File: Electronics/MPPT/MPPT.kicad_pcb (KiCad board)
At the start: 2 copper layers, 152.4 x 119.4 mm, 128 parts, among them J1 Solar Array, J2 Battery, J3 Car Power, J4 CAN_In, J5 CAN_Out, Q1 200N25N, Q2 200N25N, SW1 RESET, SW2 CAN Address, U1 PQMC3-D12-S9-S, U2 Nucleo_L432KC, U3 UCC37321, U4 INA210, U5 ADM3055E, U6 INA210, U7 CDSOT23-T24CAN

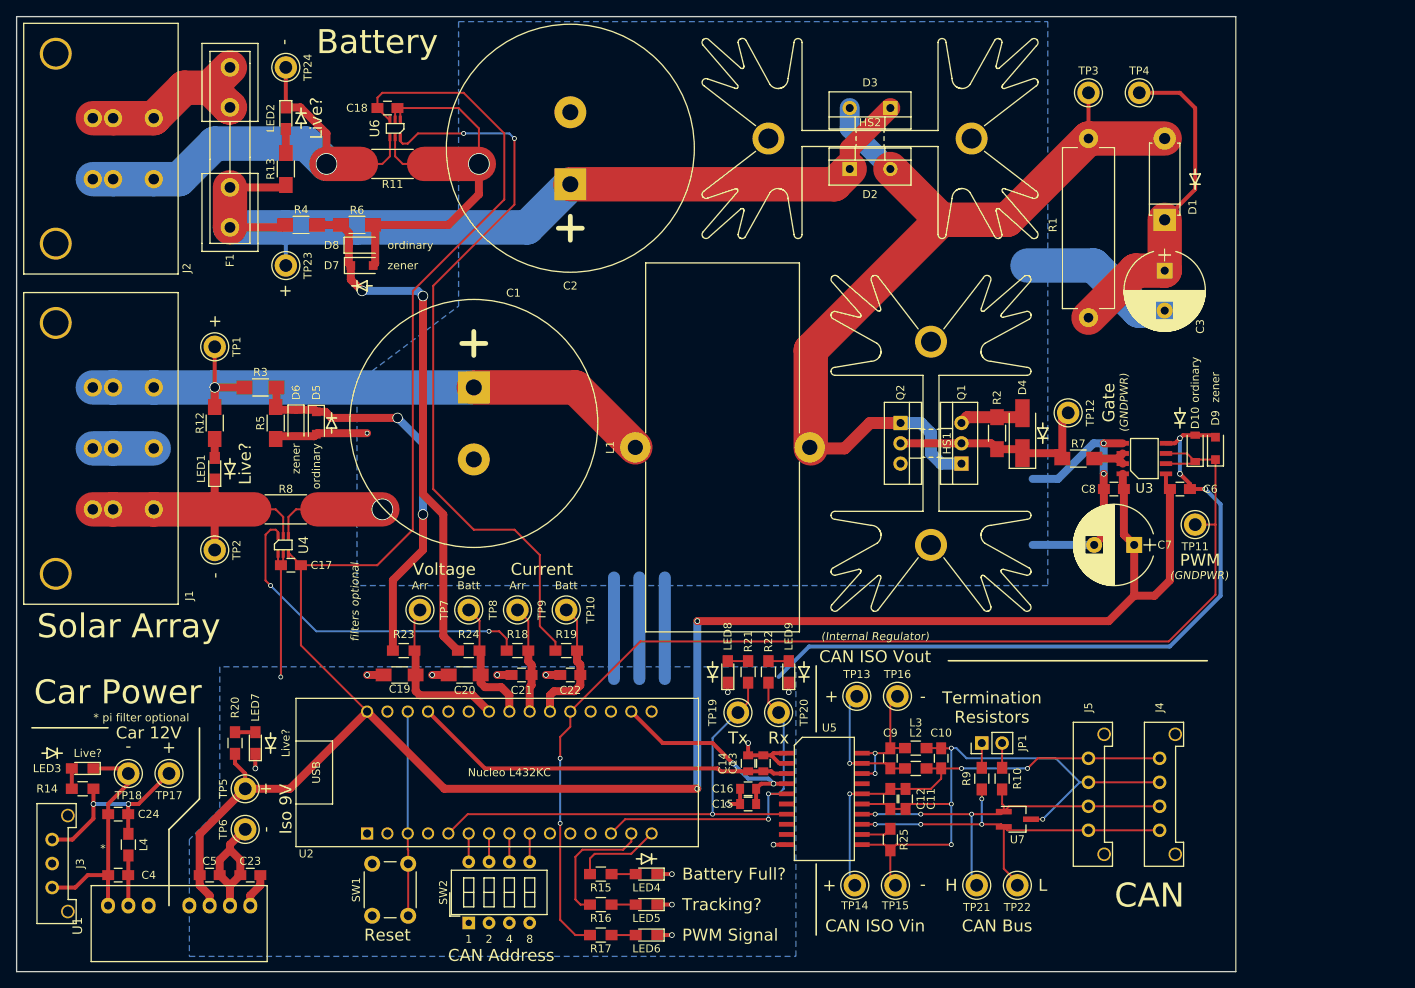
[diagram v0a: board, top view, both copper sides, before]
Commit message: MPPT: Fill GND planes
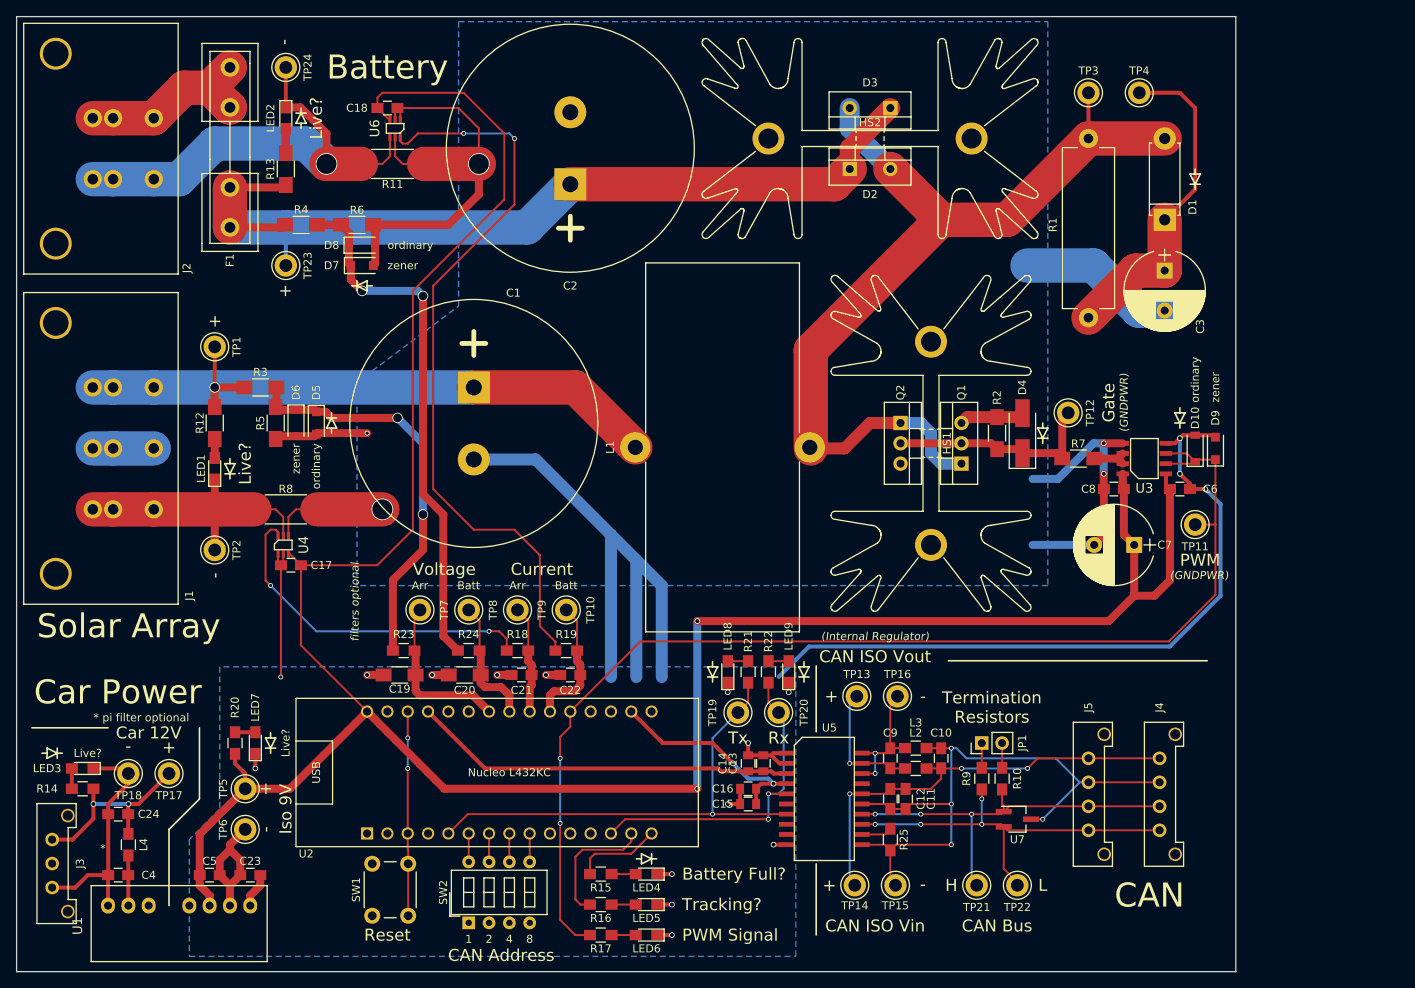
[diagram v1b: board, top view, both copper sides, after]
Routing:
- net GNDPWR: track 297.7 -> 372.2 mm
- net (no net): track 38.1 -> 0.00 mm
- net /Reset: vias 0 -> 2

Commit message: MPPT: Further compact board
Saved ~.6 sq in
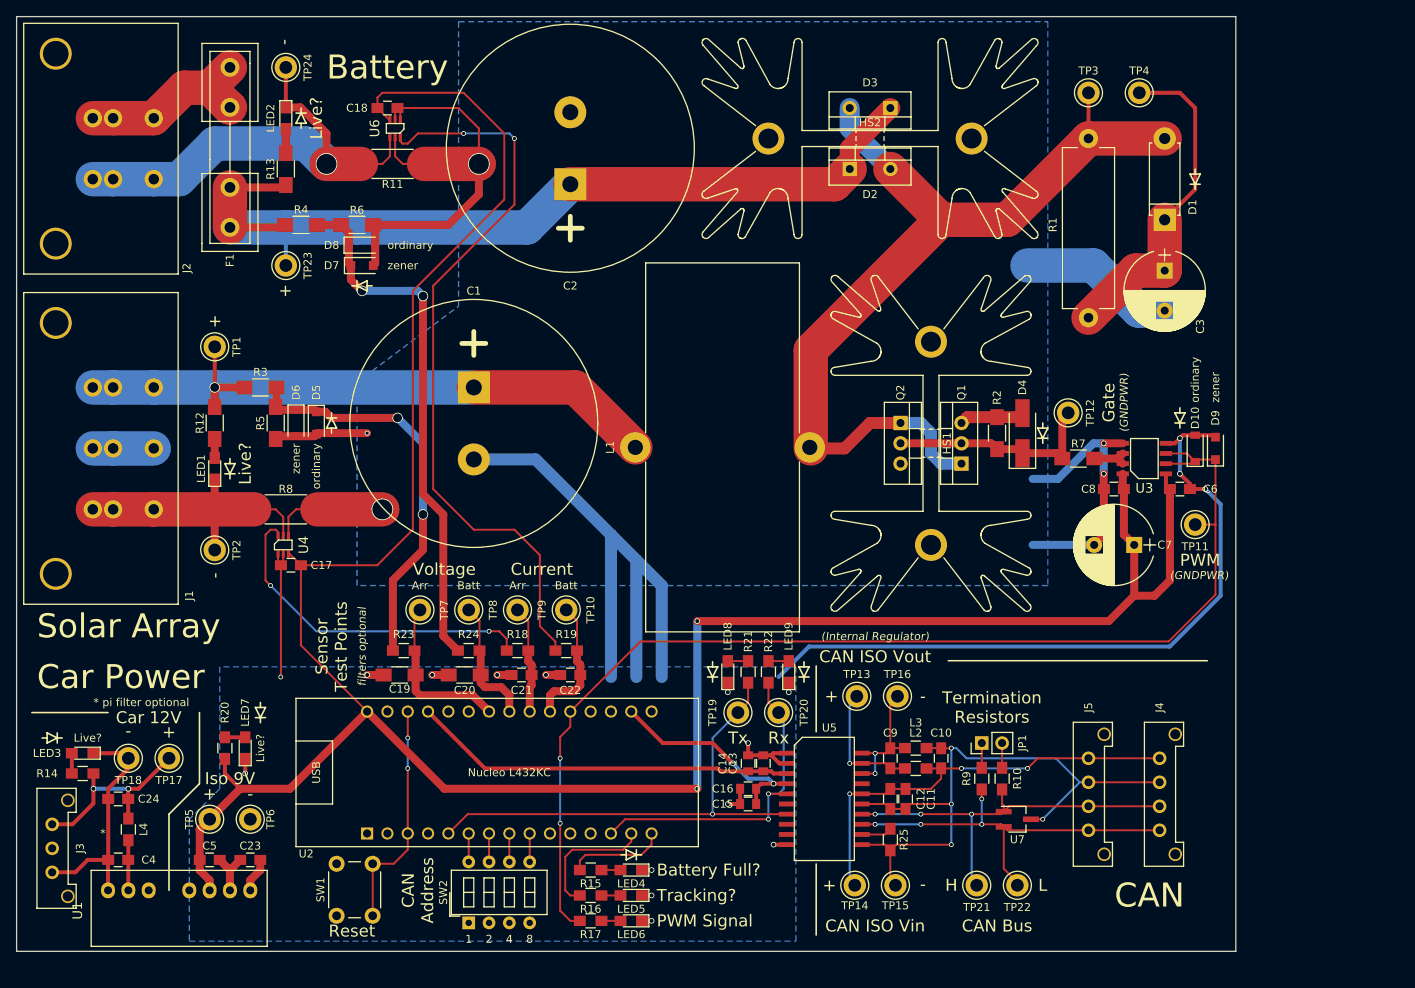
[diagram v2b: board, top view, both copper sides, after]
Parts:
- moved TP5 5.85 mm to (55.2, 131.4), turned to 180 degrees
- moved SW1 4.44 mm to (71.1, 143.5)
- moved REF** 4.02 mm to (61.6, 118.1)
- moved LED6 2.61 mm to (108.0, 144.1)
- moved LED5 2.22 mm to (108.0, 141.0)
- moved R17 2.18 mm to (102.9, 144.1)
- moved LED4 1.97 mm to (108.0, 137.8)
- moved REF** 1.97 mm to (108.0, 135.9)
- moved C23 1.91 mm to (60.3, 136.5)
- moved C24 1.91 mm to (43.8, 128.9)
- moved C4 1.91 mm to (43.8, 136.5)
- moved C5 1.91 mm to (55.2, 136.5)
- moved J3 1.91 mm to (35.6, 132.1)
- moved L4 1.91 mm to (45.1, 132.7)
- moved LED3 1.91 mm to (39.4, 123.2)
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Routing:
- net GNDPWR: track 372.2 -> 359.5 mm
- net /Reset: track 25.5 -> 28.9 mm
- net /PWM: track 147.7 -> 145.0 mm
- net +9VA: track 314.0 -> 312.1 mm
- net /Battery_Full: track 10.9 -> 12.4 mm
- net Net-(LED6-Pad2): track 3.02 -> 2.38 mm
- net Net-(LED5-Pad2): track 3.02 -> 2.38 mm
- net Net-(LED4-Pad2): track 3.02 -> 2.38 mm
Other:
- board size 152.4 x 119.4 mm -> 152.4 x 116.8 mm
- board text added: "Sensor Test Points"

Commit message: MPPT: Add ground TPs for sensors, snubber, and FET driver.
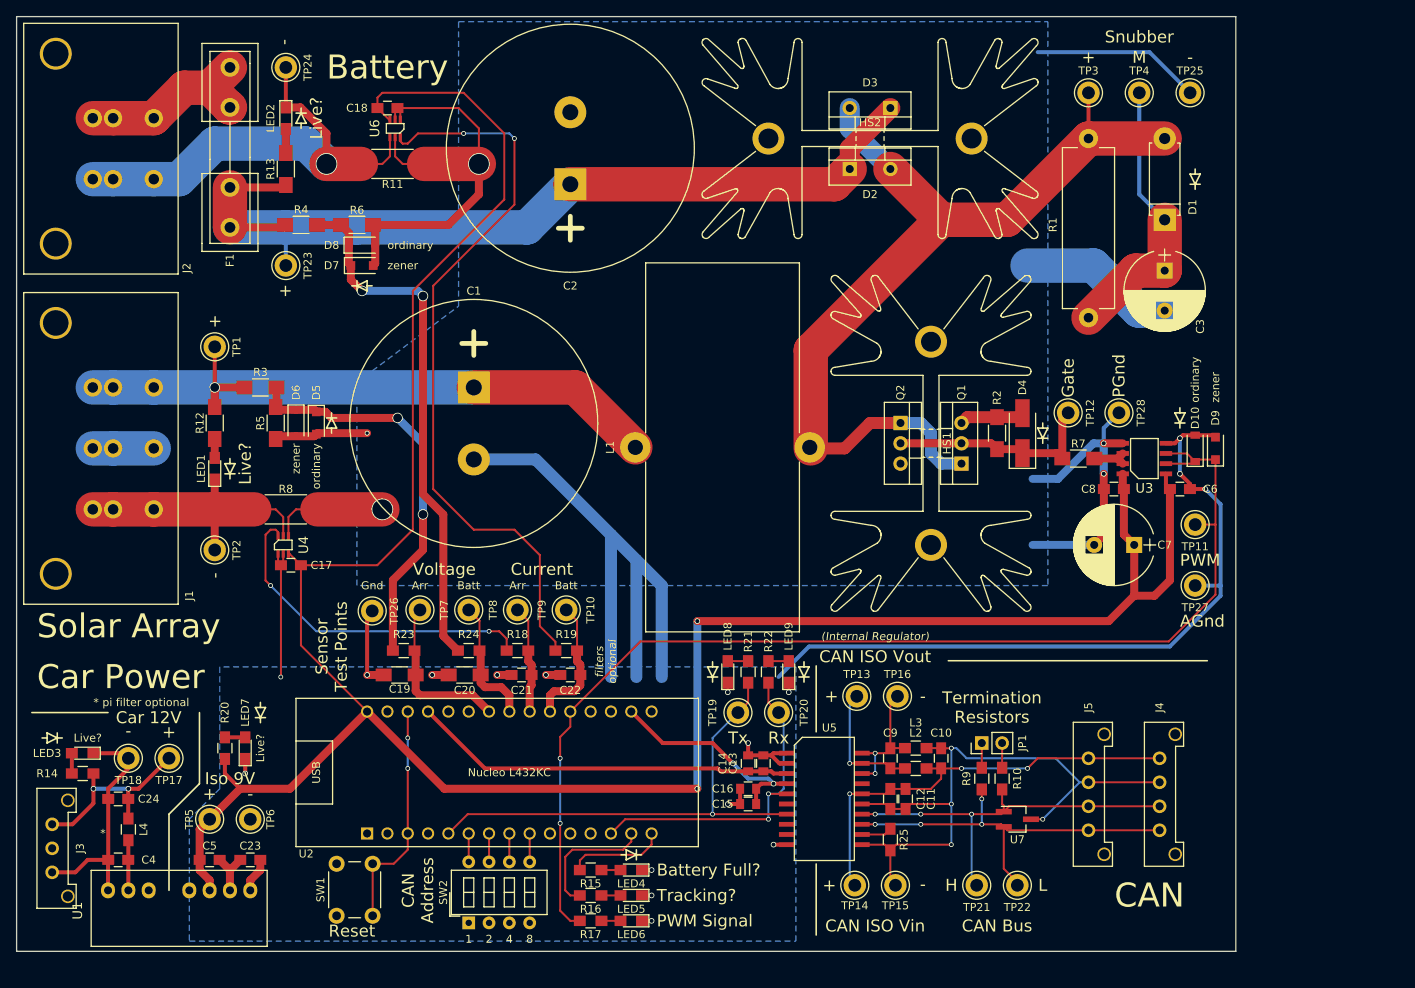
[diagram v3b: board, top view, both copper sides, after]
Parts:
- added TP25: -SNUB, Measurement_Points:Test_Point_Keystone_5005-5009_Compact, F.Cu at (177.8, 40.6)
- added TP26: GND, Measurement_Points:Test_Point_Keystone_5005-5009_Compact, F.Cu at (75.6, 105.4)
- added TP27: AGND, Measurement_Points:Test_Point_Keystone_5005-5009_Compact, F.Cu at (178.4, 102.2)
- added TP28: PGND, Measurement_Points:Test_Point_Keystone_5005-5009_Compact, F.Cu at (168.9, 80.6)
- TP4: value SNUB_MID -> M_SNUB
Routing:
- net GNDPWR: track 359.5 -> 396.7 mm
- net Net-(C3-Pad1): track 41.6 -> 35.5 mm
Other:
- board text added: "AGnd"
- board text added: "Gnd"
- board text added: "M"
- board text added: "PGnd"
- board text added: "Snubber"
- board text removed: "(GNDPWR)"

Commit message: MPPT: Use more appropriate footprints for snubber components; rearrange that portion of board.
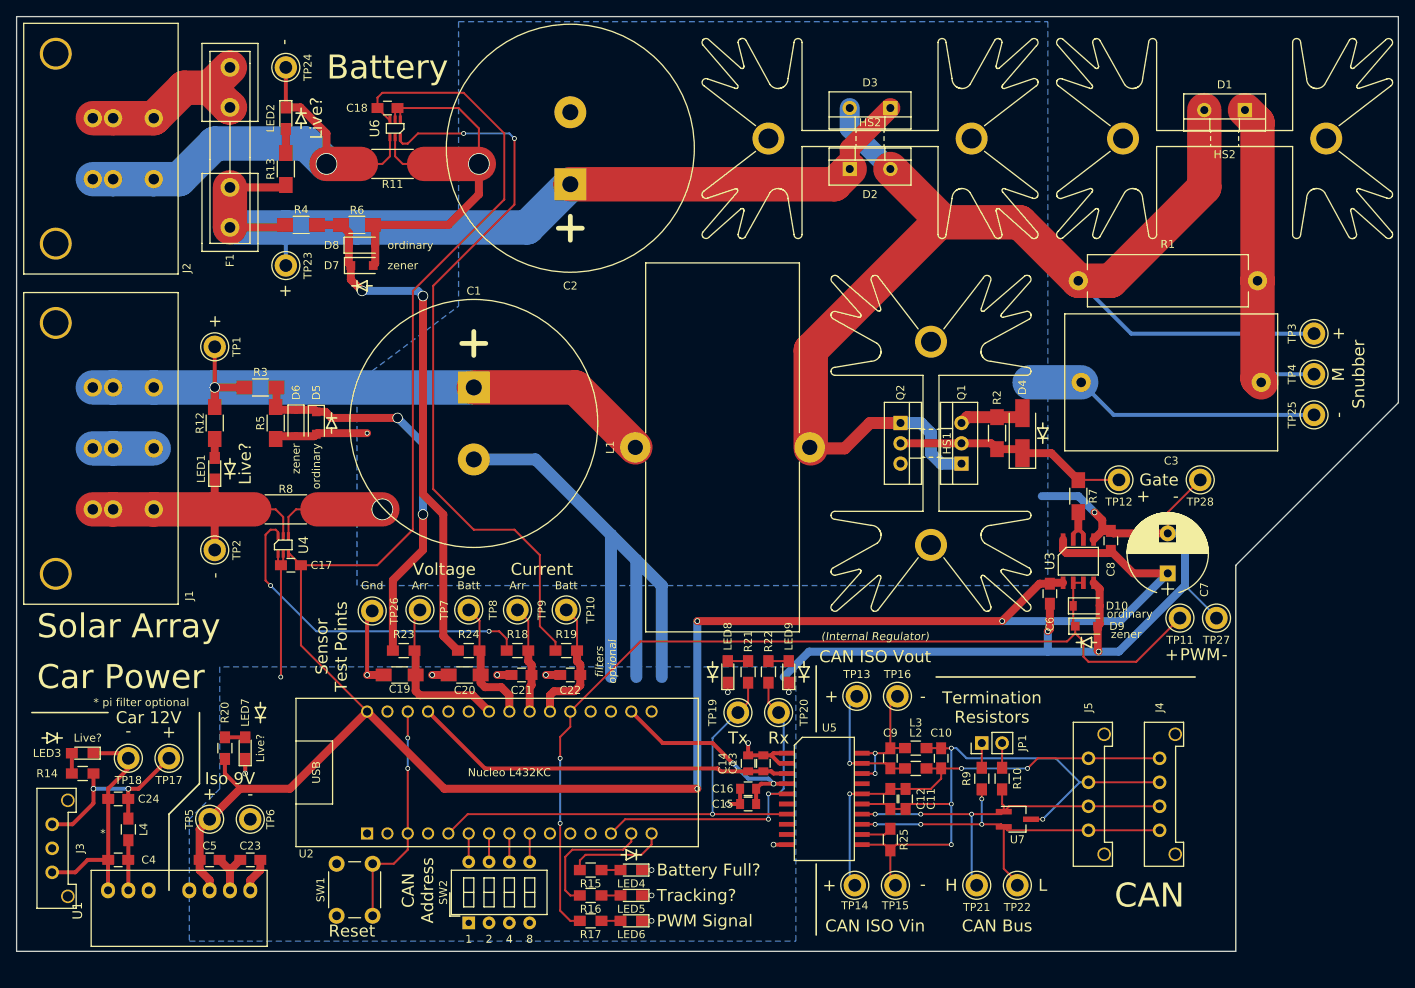
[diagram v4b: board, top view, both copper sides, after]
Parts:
- removed the REF** at (178.4, 51.4)
- added HS2: Heatsink_Fischer_SK129-STS_42x25mm_2xDrill2.5mm, Heatsinks:Heatsink_Fischer_SK129-STS_42x25mm_2xDrill2.5mm, F.Cu at (182.1, 46.4)
- C3: footprint Capacitors_THT:CP_Radial_D10.0mm_P5.00mm -> MPPT_Custom:C_Rect_L26.5mm_W17.0mm_P22.50mm_MKS4
- D1: value Diode -> Schottky; footprint Diodes_THT:D_5W_P10.16mm_Horizontal -> TO_SOT_Packages_THT:TO-220-2_Vertical
- moved TP25 43.1 mm to (193.3, 80.9), turned to 90 degrees
- moved TP4 41.4 mm to (193.3, 75.8), turned to 90 degrees
- moved TP3 41.2 mm to (193.3, 70.7), turned to 90 degrees
- moved REF** 30.4 mm to (164.8, 109.3), turned to 90 degrees
- moved D9 27.5 mm to (164.8, 107.3), turned to 0 degrees
- moved D10 23.9 mm to (164.8, 104.8), turned to 0 degrees
- moved C6 20.9 mm to (160.3, 103.3), turned to 90 degrees
- moved C3 18.5 mm to (186.7, 76.8), turned to 180 degrees
- moved R1 17.8 mm to (163.8, 64.1), turned to 0 degrees
- moved D1 17.0 mm to (184.7, 42.8), turned to 180 degrees
- moved U3 15.3 mm to (163.8, 99.2), turned to 0 degrees
- moved TP28 13.2 mm to (179.1, 89.0), turned to 180 degrees
- moved TP11 11.8 mm to (176.5, 106.3)
- moved TP12 10.5 mm to (168.9, 89.0), turned to 180 degrees
- moved C8 6.49 mm to (167.9, 96.6), turned to 90 degrees
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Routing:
- net Net-(D1-Pad2): track 115.6 -> 160.7 mm
- net /PWM: track 145.0 -> 121.2 mm
- net GNDPWR: track 396.7 -> 374.8 mm, vias 22 -> 20
- net Net-(C3-Pad1): track 35.5 -> 41.9 mm
- net +9VA: track 312.1 -> 308.3 mm, vias 2 -> 3
- net /Drive_PWM: track 27.1 -> 29.2 mm
- net Net-(R7-Pad2): track 4.72 -> 5.32 mm
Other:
- board size 152.4 x 116.8 mm -> 172.7 x 116.8 mm
- board text removed: "AGnd"
- board text removed: "PGnd"

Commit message: MPPT: Correct fuse footprint.
We had been using a placeholder for a while, but I've now verified the correct footprint.
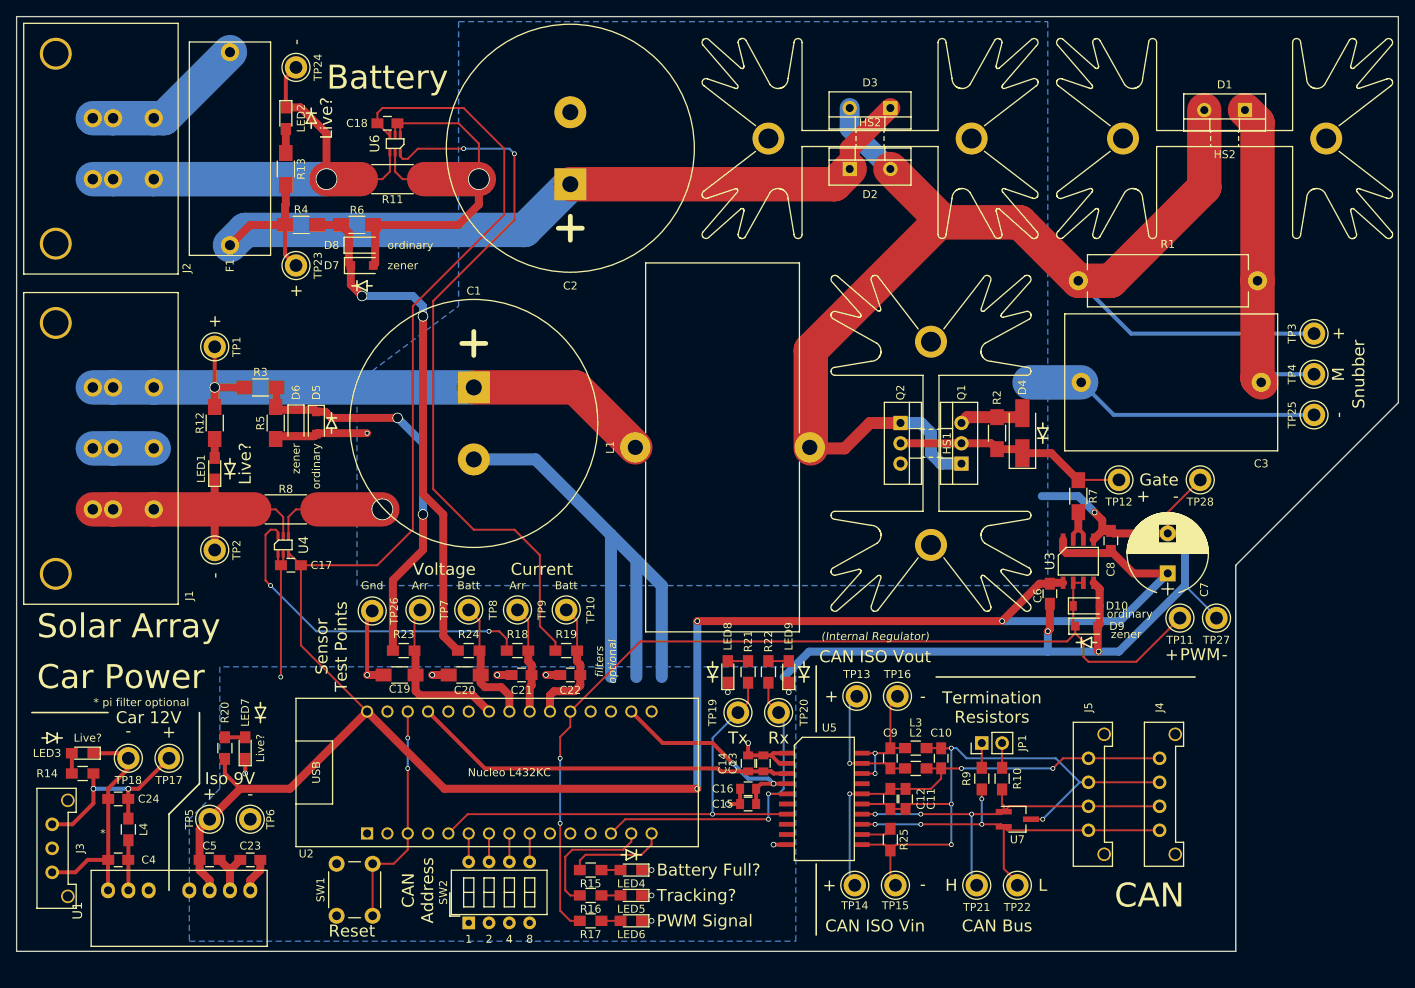
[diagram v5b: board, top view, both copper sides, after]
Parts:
- F1: footprint Fuse_Holders_and_Fuses:Fuseholder5x20_horiz_open_inline_Type-I -> UTSVT_Passive:LittelFuse_OMNIBLOK_520Series_PCB
- moved F1 10.2 mm to (57.8, 47.6)
- moved C18 1.91 mm to (77.5, 44.5)
- moved R11 1.91 mm to (78.1, 51.4)
- moved U6 1.91 mm to (78.4, 47.0)
- moved TP23 1.27 mm to (66.0, 62.2)
- moved TP24 1.27 mm to (66.0, 37.5)
- moved REF** 1.27 mm to (67.9, 43.8)
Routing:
- net /+Batt: track 114.7 -> 110.2 mm
- net Net-(F1-Pad1): track 23.3 -> 20.6 mm
- net Net-(R19-Pad1): track 93.2 -> 91.3 mm
- net +9VA: track 308.3 -> 306.4 mm
- net GNDPWR: track 374.8 -> 373.6 mm
